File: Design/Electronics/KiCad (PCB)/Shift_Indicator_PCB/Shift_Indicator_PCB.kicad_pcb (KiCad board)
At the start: 2 copper layers, 99 x 68 mm, 31 parts, among them J1 Arduino Connector, J13 OBDII Connector, J2 GND, J3 Batt, J4 LIN

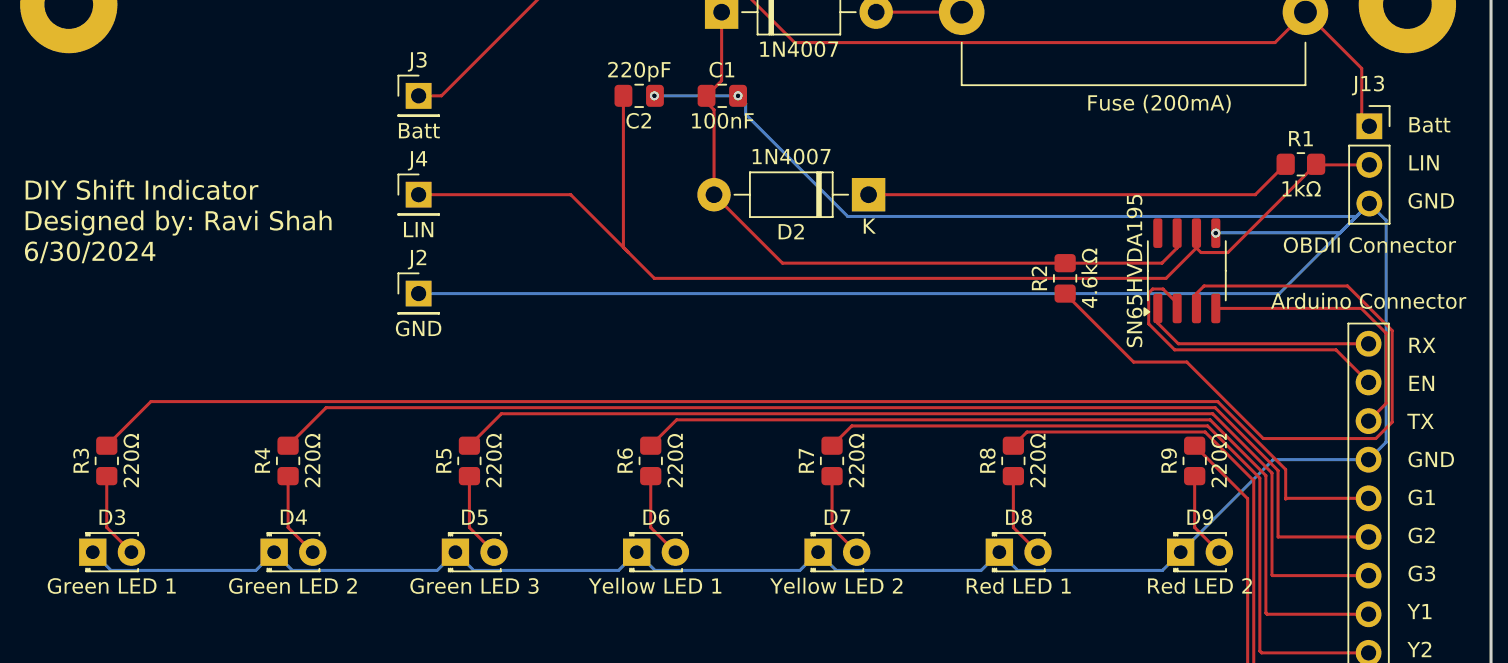
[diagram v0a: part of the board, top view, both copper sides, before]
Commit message: fix PCB for approval + netlist/BOM
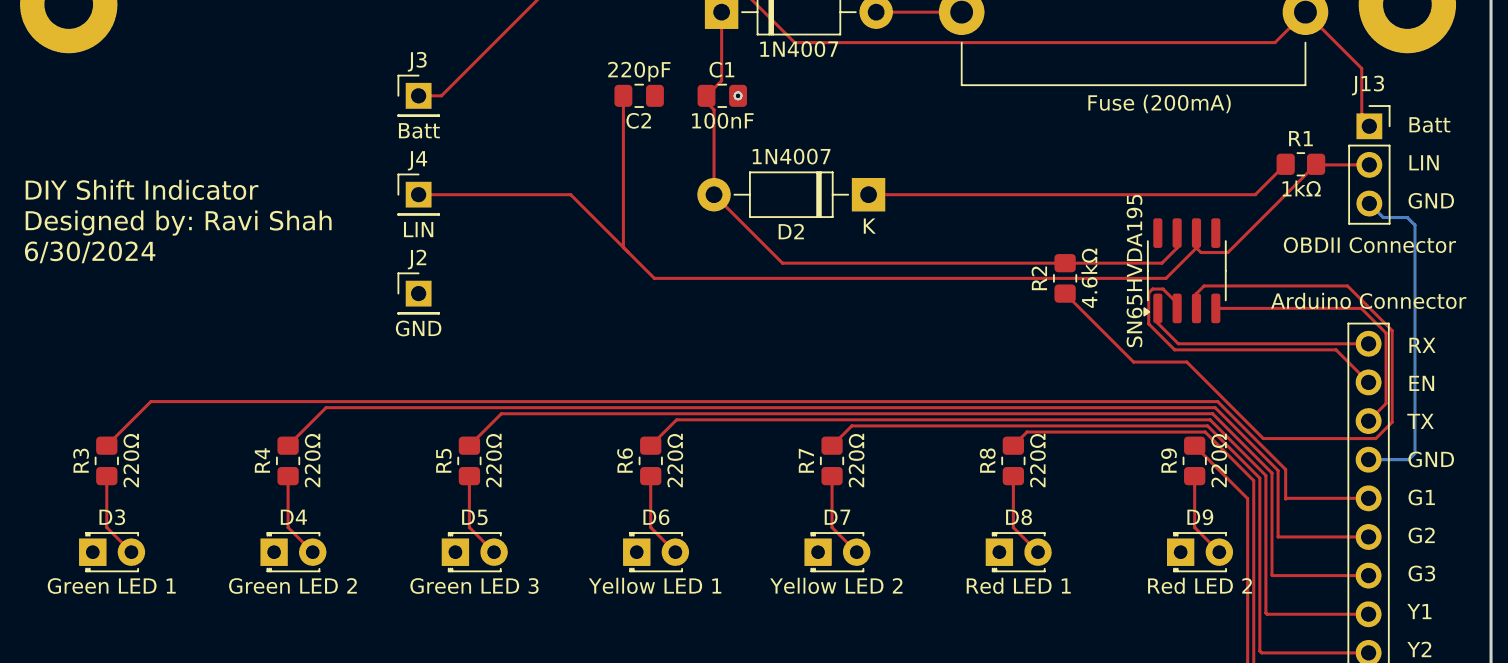
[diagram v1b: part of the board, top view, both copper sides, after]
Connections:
- net -BATT renamed +BATT
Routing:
- net GND: track 237.4 -> 22.2 mm, vias 3 -> 1
